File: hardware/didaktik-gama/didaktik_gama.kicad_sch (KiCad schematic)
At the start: 174 parts, among them J1 Klávesnice, J2 MG, J3 TV, J4 Porty 8255, J5 Napájení 9–12V DC, J6 Video (cinch), SW1 RESET, T1 KSY72, T2 KSY72, T3 KC507, T4 KC507 (BC547), T5 KC507 (ZTX313), T6 KC507 (ZTX313), U1 UA880D (Z80), U10 4164, U11 4164, U12 4164, U13 4164, U14 4164, U15 4164, U16 4164, U17 2118, U18 2118, U19 2118, U2 27128 (16K EPROM), U20 2118, U21 2118, U22 2118, U23 2118, U24 2118, U25 74LS04, U26 74LS04, U27 74LS00, U28 74LS10, U29 74LS32, U3 8255 (MHB8255), U30 LM1889, U31 VF modulátor (UM1233 nebo ekv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, U32 MA7805, U4 ULA, U5 74LS157, U6 74LS157, U7 74LS157, U8 74LS157, U9 4164, Y1 14MHz, Y2 4.433619MHz

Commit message: Transcribe LM1889 coder surroundings from ZX Spectrum Issue 1/2 schematic
Level shifters with VR1/VR2, 4.8V chroma bias divider, crystal oscillator
and lead/lag network, TR1/TR2 luma+chroma summing and emitter follower,
15R-fed modulator supply; values from the Spectrum parts list.

Co-Authored-By: Claude Opus 5.5 <noreply@anthropic.com>
Claude-Session: https://claude.ai/code/session_01LAVM7Gq9EYiUXiCEdy9ZRx
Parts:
- removed C12, C20, C21, C22, C23, C24, C25, C26, C27, C30, C31, C32, C33, C34: 100n, Capacitor_THT:C_Disc_D5.0mm_W2.5mm_P5.00mm, symbol gama:C
- removed C65: 5–30p trimr (TC2), Capacitor_THT:C_Disc_D5.0mm_W2.5mm_P5.00mm, symbol gama:C
- removed R37, R41: 8k2, Resistor_THT:R_Axial_DIN0207_L6.3mm_D2.5mm_P10.16mm_Horizontal, symbol gama:R
- removed R53, R56: 1k, Resistor_THT:R_Axial_DIN0207_L6.3mm_D2.5mm_P10.16mm_Horizontal, symbol gama:R
- removed R54: 100, Resistor_THT:R_Axial_DIN0207_L6.3mm_D2.5mm_P10.16mm_Horizontal, symbol gama:R
- removed U23: 2118, Package_DIP:DIP-16_W7.62mm, symbol gama:2118
- removed unit 3 of U25
- removed U32: MA7805, Package_TO_SOT_THT:TO-220-3_Vertical, symbol gama:7805
- added C36, C37, C38, C39, C40, C41, C42, C43, C44, C45, C46, C47, C48: 100n, Capacitor_THT:C_Disc_D5.0mm_W2.5mm_P5.00mm, symbol gama:C
- added C60, C61: 47u/10V, Capacitor_THT:CP_Radial_D5.0mm_P2.00mm, symbol gama:CP
- added C65: 22u/16V (Sp C34), Capacitor_THT:CP_Radial_D5.0mm_P2.00mm, symbol gama:CP
- added C71: 33p (Sp C38), Capacitor_THT:C_Disc_D5.0mm_W2.5mm_P5.00mm, symbol gama:C
- added C72: 10n (Sp C39), Capacitor_THT:C_Disc_D5.0mm_W2.5mm_P5.00mm, symbol gama:C
- added C73: 22u/16V (Sp C65), Capacitor_THT:CP_Radial_D5.0mm_P2.00mm, symbol gama:CP
- added C74: 47n (Sp C61), Capacitor_THT:C_Disc_D5.0mm_W2.5mm_P5.00mm, symbol gama:C
- added C75: 22u/16V (Sp C25), Capacitor_THT:CP_Radial_D5.0mm_P2.00mm, symbol gama:CP
- added R26: 470, Resistor_THT:R_Axial_DIN0207_L6.3mm_D2.5mm_P10.16mm_Horizontal, symbol gama:R
- added R52: 2K2 trimr (Sp VR2), Resistor_THT:R_Axial_DIN0207_L6.3mm_D2.5mm_P10.16mm_Horizontal, symbol gama:R
- added R58: 3K (Sp R43), Resistor_THT:R_Axial_DIN0207_L6.3mm_D2.5mm_P10.16mm_Horizontal, symbol gama:R
- added R59: 5K1 (Sp R44), Resistor_THT:R_Axial_DIN0207_L6.3mm_D2.5mm_P10.16mm_Horizontal, symbol gama:R
- added R60: 1K (Sp R45), Resistor_THT:R_Axial_DIN0207_L6.3mm_D2.5mm_P10.16mm_Horizontal, symbol gama:R
- added R61: 1K (Sp R46), Resistor_THT:R_Axial_DIN0207_L6.3mm_D2.5mm_P10.16mm_Horizontal, symbol gama:R
- added R62: 10K (Sp R72), Resistor_THT:R_Axial_DIN0207_L6.3mm_D2.5mm_P10.16mm_Horizontal, symbol gama:R
- added R63: 220R (Sp R47), Resistor_THT:R_Axial_DIN0207_L6.3mm_D2.5mm_P10.16mm_Horizontal, symbol gama:R
- added R64: 4K7 (Sp R48), Resistor_THT:R_Axial_DIN0207_L6.3mm_D2.5mm_P10.16mm_Horizontal, symbol gama:R
- added R65: 4K7 (Sp R50), Resistor_THT:R_Axial_DIN0207_L6.3mm_D2.5mm_P10.16mm_Horizontal, symbol gama:R
- added R66: 18K (Sp R49), Resistor_THT:R_Axial_DIN0207_L6.3mm_D2.5mm_P10.16mm_Horizontal, symbol gama:R
- added R67: 2K2 (Sp R52), Resistor_THT:R_Axial_DIN0207_L6.3mm_D2.5mm_P10.16mm_Horizontal, symbol gama:R
- added R68: 2K2 (Sp R51), Resistor_THT:R_Axial_DIN0207_L6.3mm_D2.5mm_P10.16mm_Horizontal, symbol gama:R
- added R69: 390R (Sp R53), Resistor_THT:R_Axial_DIN0207_L6.3mm_D2.5mm_P10.16mm_Horizontal, symbol gama:R
- added R70: 15R (Sp R64), Resistor_THT:R_Axial_DIN0207_L6.3mm_D2.5mm_P10.16mm_Horizontal, symbol gama:R
- added T5: KC507 (Sp TR1 ZTX313), Package_TO_SOT_THT:TO-18-3, symbol gama:NPN
- added unit 5 of U27
- added unit 1 of U29
- added unit 4 of U29
- added Y2: 4.433619MHz (Sp X2), Crystal:Crystal_HC49-4H_Vertical, symbol gama:XTAL
- C34: renamed from C60; value 47u/10V -> 100n; footprint Capacitor_THT:CP_Radial_D5.0mm_P2.00mm -> Capacitor_THT:C_Disc_D5.0mm_W2.5mm_P5.00mm; symbol gama:CP -> gama:C
- C35: renamed from C61; value 47u/10V -> 100n; footprint Capacitor_THT:CP_Radial_D5.0mm_P2.00mm -> Capacitor_THT:C_Disc_D5.0mm_W2.5mm_P5.00mm; symbol gama:CP -> gama:C
- C64: value 100n -> 47n (Sp C33)
- C66: value 150p -> 47n (Sp C40)
- C67: value 150p -> trimr (Sp VC2)
- C68: value 1n -> 33p (Sp C37)
- R37: renamed from U27; value 74LS00 -> 8k2; footprint Package_DIP:DIP-14_W7.62mm -> Resistor_THT:R_Axial_DIN0207_L6.3mm_D2.5mm_P10.16mm_Horizontal; symbol gama:7400 -> gama:R
- R41: renamed from U29; value 74LS32 -> 8k2; footprint Package_DIP:DIP-14_W7.62mm -> Resistor_THT:R_Axial_DIN0207_L6.3mm_D2.5mm_P10.16mm_Horizontal; symbol gama:7432 -> gama:R
- R48: value 1k -> 3K3 (Sp R38)
- R49: value 2k2 trimr (VR1) -> 2K2 trimr (Sp VR1)
- R50: value 1k -> 220R (Sp R56)
- R51: value 2k2 trimr (VR2) -> 3K3 (Sp R39)
- R53: renamed from Y2; value 4.433619MHz -> 330R (Sp R57); footprint Crystal:Crystal_HC49-4H_Vertical -> Resistor_THT:R_Axial_DIN0207_L6.3mm_D2.5mm_P10.16mm_Horizontal; symbol gama:XTAL -> gama:R
- R54: renamed from R52; value 1k -> 1K (Sp R40)
- R55: value 1k -> 1K5 (Sp R41)
- R56: renamed from T5; value KC507 (ZTX313) -> 1K (Sp R42); footprint Package_TO_SOT_THT:TO-18-3 -> Resistor_THT:R_Axial_DIN0207_L6.3mm_D2.5mm_P10.16mm_Horizontal; symbol gama:NPN -> gama:R
- T6: value KC507 (ZTX313) -> KC507 (Sp TR2 ZTX313)
- U23: renamed from R26; value 470 -> 2118; footprint Resistor_THT:R_Axial_DIN0207_L6.3mm_D2.5mm_P10.16mm_Horizontal -> Package_DIP:DIP-16_W7.62mm; symbol gama:R -> gama:2118
- U25: renamed from U29; value 74LS32 -> 74LS04; symbol gama:7432 -> gama:7404
- U30: value LM1889 -> LM1889N
- U32: renamed from C29; value 100n -> MA7805; footprint Capacitor_THT:C_Disc_D5.0mm_W2.5mm_P5.00mm -> Package_TO_SOT_THT:TO-220-3_Vertical; symbol gama:C -> gama:7805
- renumbered C28 to C12, C35 to C20, C36 to C21, C37 to C22, C38 to C23, C39 to C24, C40 to C25, C41 to C26, C42 to C27, C43 to C28, C44 to C29, C45 to C30, C46 to C31, C47 to C32, C48 to C33
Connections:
- net CH_XT is gone; now on net GND: R53.2
- net +12V: now also C64.1, C66.1, R48.1, R51.1, R55.1, R56.1; no longer U30.12 (VIDEO)
- net +5V: now also R37.1, R41.1, U23.8 (VCC), U23.9 (VCC), U32.3 (OUT), C36.1, C37.1, C38.1, C39.1, C40.1, C41.1, C42.1, C43.1, C44.1, C45.1, C46.1, C47.1, C48.1, C60.1, C61.1, R62.1, R70.1, U27.14 (VCC); no longer C12.1, R37.14 (VCC), R55.1, T6.3 (C), U31.2 (+5V), U32.1
- net A7: now also U25.5
- net A7_N: now also U25.6
- net CBIAS: now also R54.1, R55.2, C65.1; no longer C64.1, R49.2, R51.2
- net CHROMA: now also C73.1, R62.2; no longer C68.1
- net CH_LAG: now also C68.1, R60.2; no longer C66.2, C67.1
- net CH_LEAD: now also C72.2; no longer C66.1, R54.2
- net CH_OSC: now also R58.1, R59.1; no longer R53.1, R54.1
- net CVBS: now also R69.1
- net D2: now also R37.2
- net D6: now also R41.2
- net D7: now also R26.1; no longer U23.1
- net GND: now also C66.2, C68.2, R50.2, R54.2, U23.16 (GND), C36.2, C37.2, C38.2, C39.2, C40.2, C41.2, C42.2, C43.2, C44.2, C45.2, C46.2, C47.2, C48.2, C60.2, C61.2, C65.2, C74.2, C75.2, R58.2, R61.2, R63.2, R65.2, R67.2, R69.2, U27.7 (GND); no longer C64.2, R37.7 (GND)
- net RY: now also C64.2, R51.2, R52.1; no longer R50.2, R51.1
- net T5_B: now also R64.2, R65.1, R66.2, T5.2 (B); no longer R56.2 (B)
- net T5_E: now also R67.1, T5.1 (E); no longer R56.1 (E)
- net U: now also R49.2, R50.1; no longer R48.1
- net V: now also R53.1, R52.2; no longer R50.1
- net VA0: now also U23.5 (A0)
- net VA1: now also U23.11 (A4)
- net VA2: now also U23.7 (A1)
- net VA3: now also U23.13 (A6)
- net VA4: now also U23.12 (A3)
- net VA5: now also U23.10 (A5)
- net VA6: now also U23.6 (A2)
- net VD6: now also U23.14 (Q), U23.2 (D)
- net VD7: now also R26.2; no longer U23.2
- net VIN: now also C12.1, U32.1 (IN)
- net Y: now also R63.1, R64.1
- net ~{MREQ}: now also U29.1, U29.13, U29.2; no longer R41.1, R41.2, U25.13
- net ~{RAS64}: now also U29.3; no longer R41.3
- net ~{VCAS}: now also U23.15 (~{CAS})
- net ~{VRAS}: now also U23.4 (~{RAS})
- net ~{VWE}: now also U23.3 (~{WE})
- net ~{WE64}: now also U29.11; no longer U25.11
- net ~{WR}: now also U29.12; no longer U25.12
- removed net CVBS_MIX: C68.2, R55.2, R56.3 (C), T6.2 (B)
- new net +5V_MOD: C74.1, C75.1, R66.1, R68.1, R70.2, T6.3 (C), U31.2 (+5V)
- new net CH_N2: C67.1, R59.2, Y2.1
- new net CH_N3: C71.1, R60.1, Y2.2
- new net CH_N4: C71.2, C72.1, R61.1
- new net LM_VIN: R56.2, U30.12 (VIDEO)
- new net T6_B: C73.2, R68.2, T5.3 (C), T6.2 (B)
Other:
- note added: "• R57, C69 (+12V): napájení LM1889 z nestabilizovaného vstupu – Spectrum vyrábí +12 V měničem TR4/TR5; u Gamy zdroj 12 V ověřit (z 9V adaptéru 12 V nebude)"
- note added: "• U30 LM1889 + okolí: překresleno ze schématu ZX Spectrum Issue 1/2 – Předloha Gamy má jen blok KÓDER – ověřit, že Gama používá stejné zapojení (typ obvodu na desce)"
- note added: "• U30 pin 16: chroma supply na +12V – Ve schématu Spectra není spoj pinu 16 jasně vidět; podle manuálu je to napájení chroma"
- note removed: "• R48–R51, C64: posun úrovně U/V (trimry VR1/VR2 2k2) – Topologie podle popisu v manuálu (Issue 2), hodnoty 1k typické – nastavit dle kap. 3.1.3 manuálu"
- note removed: "• R57, C69 (+12V): napájení LM1889 z nestabilizovaného vstupu – Spectrum vyrábí +12 V měničem TR4/TR5; u Gamy zdroj 12 V ověřit (při 9V adaptéru nestačí)"
- note removed: "• T5, T6, R53–R56, C68: sčítání jasu a barvy do CVBS – Podle popisu v manuálu (TR1/TR2 ZTX313); hodnoty typické, ověřit"
- note removed: "• U30 LM1889: piny podle servisního manuálu ZX Spectrum 48K (kap. 7.1) – Typ kodéru u Gamy ověřit na desce; piny 12/14/15 na +12V podle tabulky napětí v manuálu"
- note removed: "• Y2, C65–C67, R52: oscilátor 4,433619 MHz a fázovací RC 1–18 – Krystal a 150p dle soupisu Spectra; přesné zapojení RC článku ze schématu Spectra ověřit"
- moved on the sheet: C12, C20, C21, C22, C23, C24, C25, C26, C27, C28, C29, C30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

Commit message: Add Spectrum-style +12V converter for the LM1889 coder
TR4 switch with feedback coil 1703 and TR5 regulator sensing +12V via
R58/R59, BA157 rectifier, +12VA filter (15R + 100u). Coder now runs from
+12VA as in the Spectrum. Negative rails omitted (no 4116 RAM in Gama).

Co-Authored-By: Claude Opus 5.5 <noreply@anthropic.com>
Claude-Session: https://claude.ai/code/session_01LAVM7Gq9EYiUXiCEdy9ZRx
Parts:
- removed C70: 100n, Capacitor_THT:C_Disc_D5.0mm_W2.5mm_P5.00mm, symbol gama:C
- removed R42: 8k2, Resistor_THT:R_Axial_DIN0207_L6.3mm_D2.5mm_P10.16mm_Horizontal, symbol gama:R
- removed unit 3 of U25
- removed unit 1 of U26
- added C76: 100n (Sp C43), Capacitor_THT:C_Disc_D5.0mm_W2.5mm_P5.00mm, symbol gama:C
- added C77: 47n (Sp C49), Capacitor_THT:C_Disc_D5.0mm_W2.5mm_P5.00mm, symbol gama:C
- added C78: 100u/16V (Sp C44), Capacitor_THT:CP_Radial_D6.3mm_P2.50mm, symbol gama:CP
- added C79: 100u/16V (Sp C45), Capacitor_THT:CP_Radial_D6.3mm_P2.50mm, symbol gama:CP
- added C80: 4u7/16V (úprava dle manuálu), Capacitor_THT:CP_Radial_D5.0mm_P2.00mm, symbol gama:CP
- added D14: BA157 (Sp D15), Diode_THT:D_DO-41_SOD81_P10.16mm_Horizontal, symbol gama:D
- added L1: Cívka SPECTRUM 1703, symbol gama:COIL1703
- added R44: 220, Resistor_THT:R_Axial_DIN0207_L6.3mm_D2.5mm_P10.16mm_Horizontal, symbol gama:R
- added R73: 270R (Sp R60, Issue 3), Resistor_THT:R_Axial_DIN0207_L6.3mm_D2.5mm_P10.16mm_Horizontal, symbol gama:R
- added R74: 15R (Sp R62), Resistor_THT:R_Axial_DIN0207_L6.3mm_D2.5mm_P10.16mm_Horizontal, symbol gama:R
- added R75: 15R (Sp R61), Resistor_THT:R_Axial_DIN0207_L6.3mm_D2.5mm_P10.16mm_Horizontal, symbol gama:R
- added T7: KF517 (Sp TR5 ZTX213), Package_TO_SOT_THT:TO-39-3, symbol gama:PNP
- added T8: KD139 (Sp TR4 ZTX651/TIP31), Package_TO_SOT_THT:TO-126-3_Vertical, symbol gama:NPN
- added unit 4 of U28
- added unit 3 of U29
- R42: renamed from U27; value 74LS00 -> 8k2; footprint Package_DIP:DIP-14_W7.62mm -> Resistor_THT:R_Axial_DIN0207_L6.3mm_D2.5mm_P10.16mm_Horizontal; symbol gama:7400 -> gama:R
- R71: renamed from R57; value 47 -> 1K8 2% (Sp R59)
- R72: renamed from C69; value 100u/16V -> 1K 2% (Sp R58); footprint Capacitor_THT:CP_Radial_D6.3mm_P2.50mm -> Resistor_THT:R_Axial_DIN0207_L6.3mm_D2.5mm_P10.16mm_Horizontal; symbol gama:CP -> gama:R
- U25: renamed from U28; value 74LS10 -> 74LS04; symbol gama:7410 -> gama:7404
- U26: renamed from U29; value 74LS32 -> 74LS04; symbol gama:7432 -> gama:7404
- U27: renamed from R44; value 220 -> 74LS00; footprint Resistor_THT:R_Axial_DIN0207_L6.3mm_D2.5mm_P10.16mm_Horizontal -> Package_DIP:DIP-14_W7.62mm; symbol gama:R -> gama:7400
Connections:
- net +12V: now also R71.1, C78.1, D14.1, R75.1; no longer C66.1, R55.1, R56.1, R71.2, R72.1, U30.14 (RF_VCC), U30.15 (SND), U30.16 (VCC)
- net +5V: now also R42.1, U27.14 (VCC), C80.1, T7.1 (E), U28.14 (VCC); no longer R42.14 (VCC), U25.14 (VCC)
- net A7: now also U25.5
- net A7_N: now also U25.6
- net BANK: now also U26.2
- net D7: now also R42.2
- net GND: now also U27.7 (GND), C76.2, C77.2, C78.2, C79.2, T8.1 (E), U28.7 (GND); no longer R42.7 (GND), U25.7 (GND)
- net MUX2: now also R44.1, U29.8; no longer U26.8, U27.1
- net MUX2_D: now also R44.2; no longer U27.2
- net PC0: now also U26.1
- net RAS_D: now also U29.9; no longer U26.9
- net VIN: now also L1.1 (PRIM); no longer R71.1
- net ~{SEL64}: now also U29.10; no longer U26.10
- new net +12VA: C66.1, C79.1, R55.1, R56.1, R75.2, U30.14 (RF_VCC), U30.15 (SND), U30.16 (VCC)
- new net CONV_DRV: C76.1, R73.2, R74.1
- new net CONV_FA: L1.3 (FB_A), R74.2
- new net CONV_FB: C80.2, R71.2, R72.1, T7.2 (B)
- new net CONV_SW: C77.1, D14.2, L1.2 (PRIM_SW), T8.3 (C)
- new net CONV_T7C: R73.1, T7.3 (C)
- new net CONV_T8B: L1.4 (FB_B), T8.2 (B)
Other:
- note added: "MĚNIČ +12 V pro kodér (podle ZX Spectra, TR4/TR5 + cívka 1703)"
- note added: "• C80, R73: úprava stability měniče z manuálu (4u7 E–B T5, R60 270R) – Doporučeno servisním manuálem Spectra pro desky Issue 2/3"
- note added: "• L1 (cívka 1703): dvě vinutí: primár VIN–spínač, zpětná vazba R74–báze T8 – Počet závitů / indukčnost cívky Sinclair 1703 schéma neuvádí; začátky vinutí (tečky) dle schématu Spectra"
- note added: "• T7, T8: náhrady ZTX213 -> KF517 (PNP), ZTX651 -> KD139/BD139 (NPN) – Pinout pouzder se liší od ZTX (E-B-C), osadit podle skutečného tranzistoru"
- note added: "• U30 pin 16: chroma supply na +12VA – Ve schématu Spectra není spoj pinu 16 jasně vidět; podle manuálu je to napájení chroma"
- note removed: "• R57, C69 (+12V): napájení LM1889 z nestabilizovaného vstupu – Spectrum vyrábí +12 V měničem TR4/TR5; u Gamy zdroj 12 V ověřit (z 9V adaptéru 12 V nebude)"
- note removed: "• U30 pin 16: chroma supply na +12V – Ve schématu Spectra není spoj pinu 16 jasně vidět; podle manuálu je to napájení chroma"
- moved on the sheet: R71

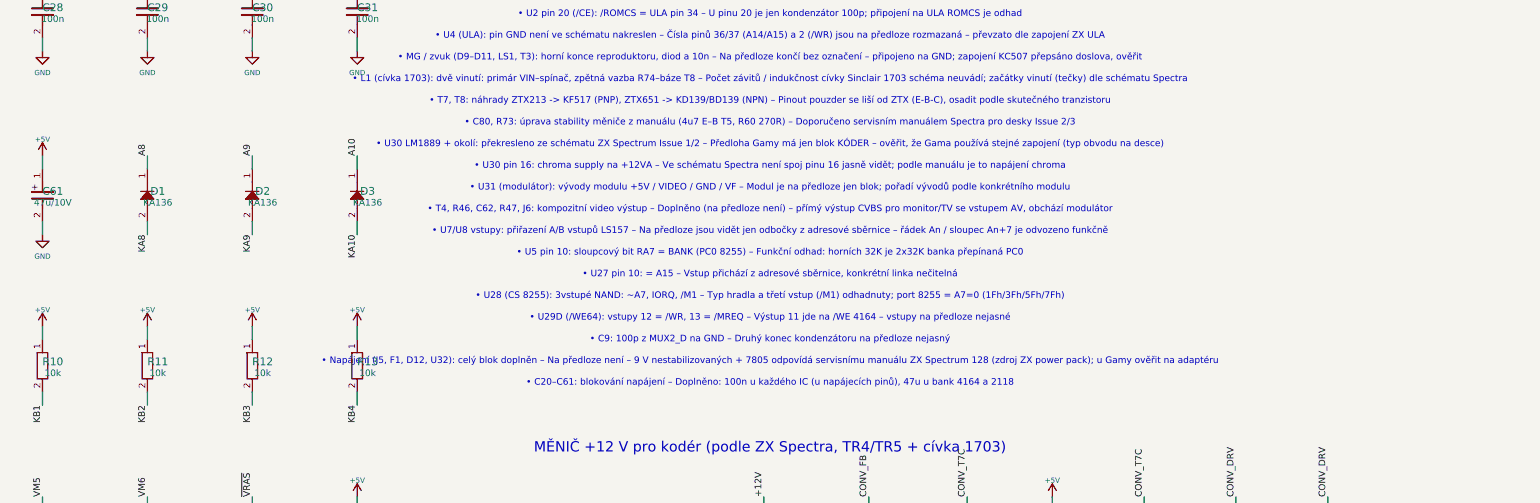
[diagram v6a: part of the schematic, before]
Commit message: Confirm KF517 as TR5 replacement from TESLA datasheet
Co-Authored-By: Claude Opus 5.5 <noreply@anthropic.com>
Claude-Session: https://claude.ai/code/session_01LAVM7Gq9EYiUXiCEdy9ZRx
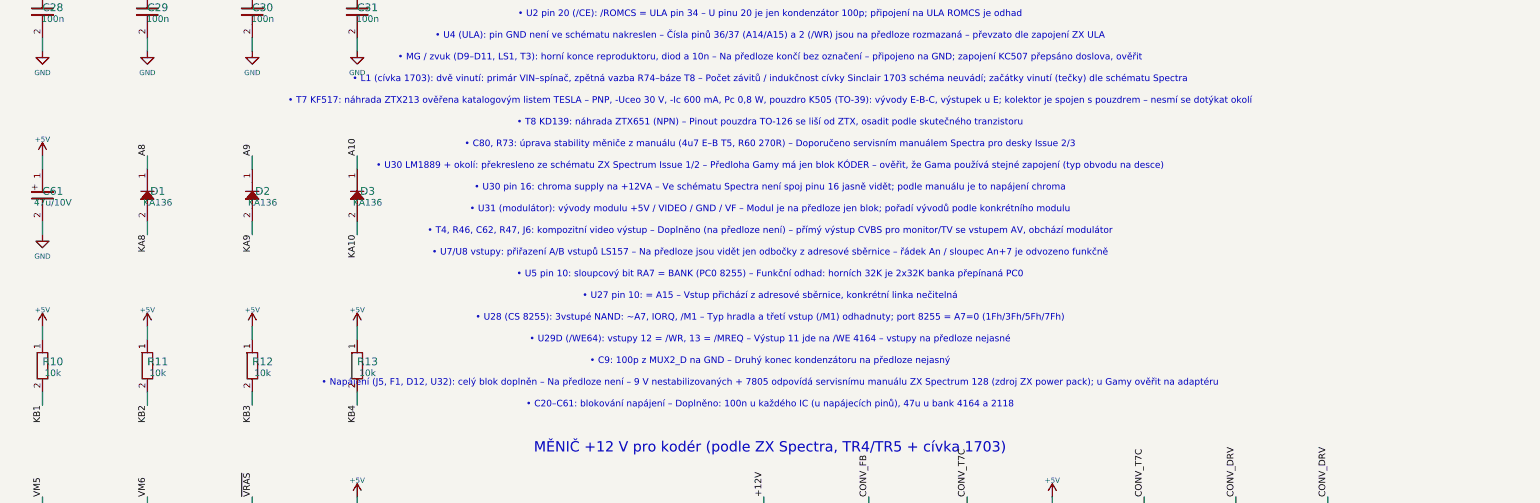
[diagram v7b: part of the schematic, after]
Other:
- note added: "• T7 KF517: náhrada ZTX213 ověřena katalogovým listem TESLA – PNP, -Uceo 30 V, -Ic 600 mA, Pc 0,8 W, pouzdro K505 (TO-39): vývody E-B-C, výstupek u E; kolektor je spojen s pouzdrem – nesmí se dotýkat okolí"
- note added: "• T8 KD139: náhrada ZTX651 (NPN) – Pinout pouzdra TO-126 se liší od ZTX, osadit podle skutečného tranzistoru"
- note removed: "• T7, T8: náhrady ZTX213 -> KF517 (PNP), ZTX651 -> KD139/BD139 (NPN) – Pinout pouzder se liší od ZTX (E-B-C), osadit podle skutečného tranzistoru"
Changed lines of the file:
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@@
         (size 1.27 1.27)))
 )
-  (text "• T7, T8: náhrady ZTX213 -> KF517 (PNP), ZTX651 -> KD139/BD139 (NPN) – Pinout pouzder se liší od ZTX (E-B-C), osadit podle skutečného tranzistoru"
+  (text "• T7 KF517: náhrada ZTX213 ověřena katalogovým listem TESLA – PNP, -Uceo 30 V, -Ic 600 mA, Pc 0,8 W, pouzdro K505 (TO-39): vývody E-B-C, výstupek u E; kolektor je spojen s pouzdrem – nesmí se dotýkat okolí"
     (at 560.00 334.80 0)
     (effects
@@
         (size 1.27 1.27)))
 )
-  (text "• C80, R73: úprava stability měniče z manuálu (4u7 E–B T5, R60 270R) – Doporučeno servisním manuálem Spectra pro desky Issue 2/3"
+  (text "• T8 KD139: náhrada ZTX651 (NPN) – Pinout pouzdra TO-126 se liší od ZTX, osadit podle skutečného tranzistoru"
     (at 560.00 339.00 0)
     (effects
@@
         (size 1.27 1.27)))
 )
-  (text "• U30 LM1889 + okolí: překresleno ze schématu ZX Spectrum Issue 1/2 – Předloha Gamy má jen blok KÓDER – ověřit, že Gama používá stejné zapojení (typ obvodu na desce)"
+  (text "• C80, R73: úprava stability měniče z manuálu (4u7 E–B T5, R60 270R) – Doporučeno servisním manuálem Spectra pro desky Issue 2/3"
     (at 560.00 343.20 0)
     (effects
@@
         (size 1.27 1.27)))
 )
-  (text "• U30 pin 16: chroma supply na +12VA – Ve schématu Spectra není spoj pinu 16 jasně vidět; podle manuálu je to napájení chroma"
+  (text "• U30 LM1889 + okolí: překresleno ze schématu ZX Spectrum Issue 1/2 – Předloha Gamy má jen blok KÓDER – ověřit, že Gama používá stejné zapojení (typ obvodu na desce)"
     (at 560.00 347.40 0)
     (effects
@@
         (size 1.27 1.27)))
 )
-  (text "• U31 (modulátor): vývody modulu +5V / VIDEO / GND / VF – Modul je na předloze jen blok; pořadí vývodů podle konkrétního modulu"
+  (text "• U30 pin 16: chroma supply na +12VA – Ve schématu Spectra není spoj pinu 16 jasně vidět; podle manuálu je to napájení chroma"
     (at 560.00 351.60 0)
     (effects
@@
         (size 1.27 1.27)))
 )
-  (text "• T4, R46, C62, R47, J6: kompozitní video výstup – Doplněno (na předloze není) – přímý výstup CVBS pro monitor/TV se vstupem AV, obchází modulátor"
+  (text "• U31 (modulátor): vývody modulu +5V / VIDEO / GND / VF – Modul je na předloze jen blok; pořadí vývodů podle konkrétního modulu"
     (at 560.00 355.80 0)
     (effects
@@
         (size 1.27 1.27)))
 )
-  (text "• U7/U8 vstupy: přiřazení A/B vstupů LS157 – Na předloze jsou vidět jen odbočky z adresové sběrnice – řádek An / sloupec An+7 je odvozeno funkčně"
+  (text "• T4, R46, C62, R47, J6: kompozitní video výstup – Doplněno (na předloze není) – přímý výstup CVBS pro monitor/TV se vstupem AV, obchází modulátor"
     (at 560.00 360.00 0)
     (effects
@@
         (size 1.27 1.27)))
 )
-  (text "• U5 pin 10: sloupcový bit RA7 = BANK (PC0 8255) – Funkční odhad: horních 32K je 2x32K banka přepínaná PC0"
+  (text "• U7/U8 vstupy: přiřazení A/B vstupů LS157 – Na předloze jsou vidět jen odbočky z adresové sběrnice – řádek An / sloupec An+7 je odvozeno funkčně"
     (at 560.00 364.20 0)
     (effects
@@
         (size 1.27 1.27)))
 )
-  (text "• U27 pin 10: = A15 – Vstup přichází z adresové sběrnice, konkrétní linka nečitelná"
+  (text "• U5 pin 10: sloupcový bit RA7 = BANK (PC0 8255) – Funkční odhad: horních 32K je 2x32K banka přepínaná PC0"
     (at 560.00 368.40 0)
     (effects
@@
         (size 1.27 1.27)))
 )
-  (text "• U28 (CS 8255): 3vstupé NAND: ~A7, IORQ, /M1 – Typ hradla a třetí vstup (/M1) odhadnuty; port 8255 = A7=0 (1Fh/3Fh/5Fh/7Fh)"
+  (text "• U27 pin 10: = A15 – Vstup přichází z adresové sběrnice, konkrétní linka nečitelná"
     (at 560.00 372.60 0)
     (effects
@@
         (size 1.27 1.27)))
 )
-  (text "• U29D (/WE64): vstupy 12 = /WR, 13 = /MREQ – Výstup 11 jde na /WE 4164 – vstupy na předloze nejasné"
+  (text "• U28 (CS 8255): 3vstupé NAND: ~A7, IORQ, /M1 – Typ hradla a třetí vstup (/M1) odhadnuty; port 8255 = A7=0 (1Fh/3Fh/5Fh/7Fh)"
     (at 560.00 376.80 0)
     (effects
@@
         (size 1.27 1.27)))
 )
-  (text "• C9: 100p z MUX2_D na GND – Druhý konec kondenzátoru na předloze nejasný"
+  (text "• U29D (/WE64): vstupy 12 = /WR, 13 = /MREQ – Výstup 11 jde na /WE 4164 – vstupy na předloze nejasné"
     (at 560.00 381.00 0)
     (effects
@@
         (size 1.27 1.27)))
 )
-  (text "• Napájení (J5, F1, D12, U32): celý blok doplněn – Na předloze není – 9 V nestabilizovaných + 7805 odpovídá servisnímu manuálu ZX Spectrum 128 (zdroj ZX power pack); u Gamy ověřit na adaptéru"
+  (text "• C9: 100p z MUX2_D na GND – Druhý konec kondenzátoru na předloze nejasný"
     (at 560.00 385.20 0)
     (effects
@@
         (size 1.27 1.27)))
 )
-  (text "• C20–C61: blokování napájení – Doplněno: 100n u každého IC (u napájecích pinů), 47u u bank 4164 a 2118"
+  (text "• Napájení (J5, F1, D12, U32): celý blok doplněn – Na předloze není – 9 V nestabilizovaných + 7805 odpovídá servisnímu manuálu ZX Spectrum 128 (zdroj ZX power pack); u Gamy ověřit na adaptéru"
     (at 560.00 389.40 0)
     (effects
       (font
+        (size 1.27 1.27)))
+)
+  (text "• C20–C61: blokování napájení – Doplněno: 100n u každého IC (u napájecích pinů), 47u u bank 4164 a 2118"
+    (at 560.00 393.60 0)
+    (effects
+      (font
